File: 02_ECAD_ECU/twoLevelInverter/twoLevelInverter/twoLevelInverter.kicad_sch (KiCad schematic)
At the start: 14 parts, among them J1 FX10A-80S_8-SV_71_, J2 43045-0812, J3 Screw_Terminal_01x04, J4 Screw_Terminal_01x04, J5 Screw_Terminal_01x02, J6 Screw_Terminal_01x02, J7 Screw_Terminal_01x02

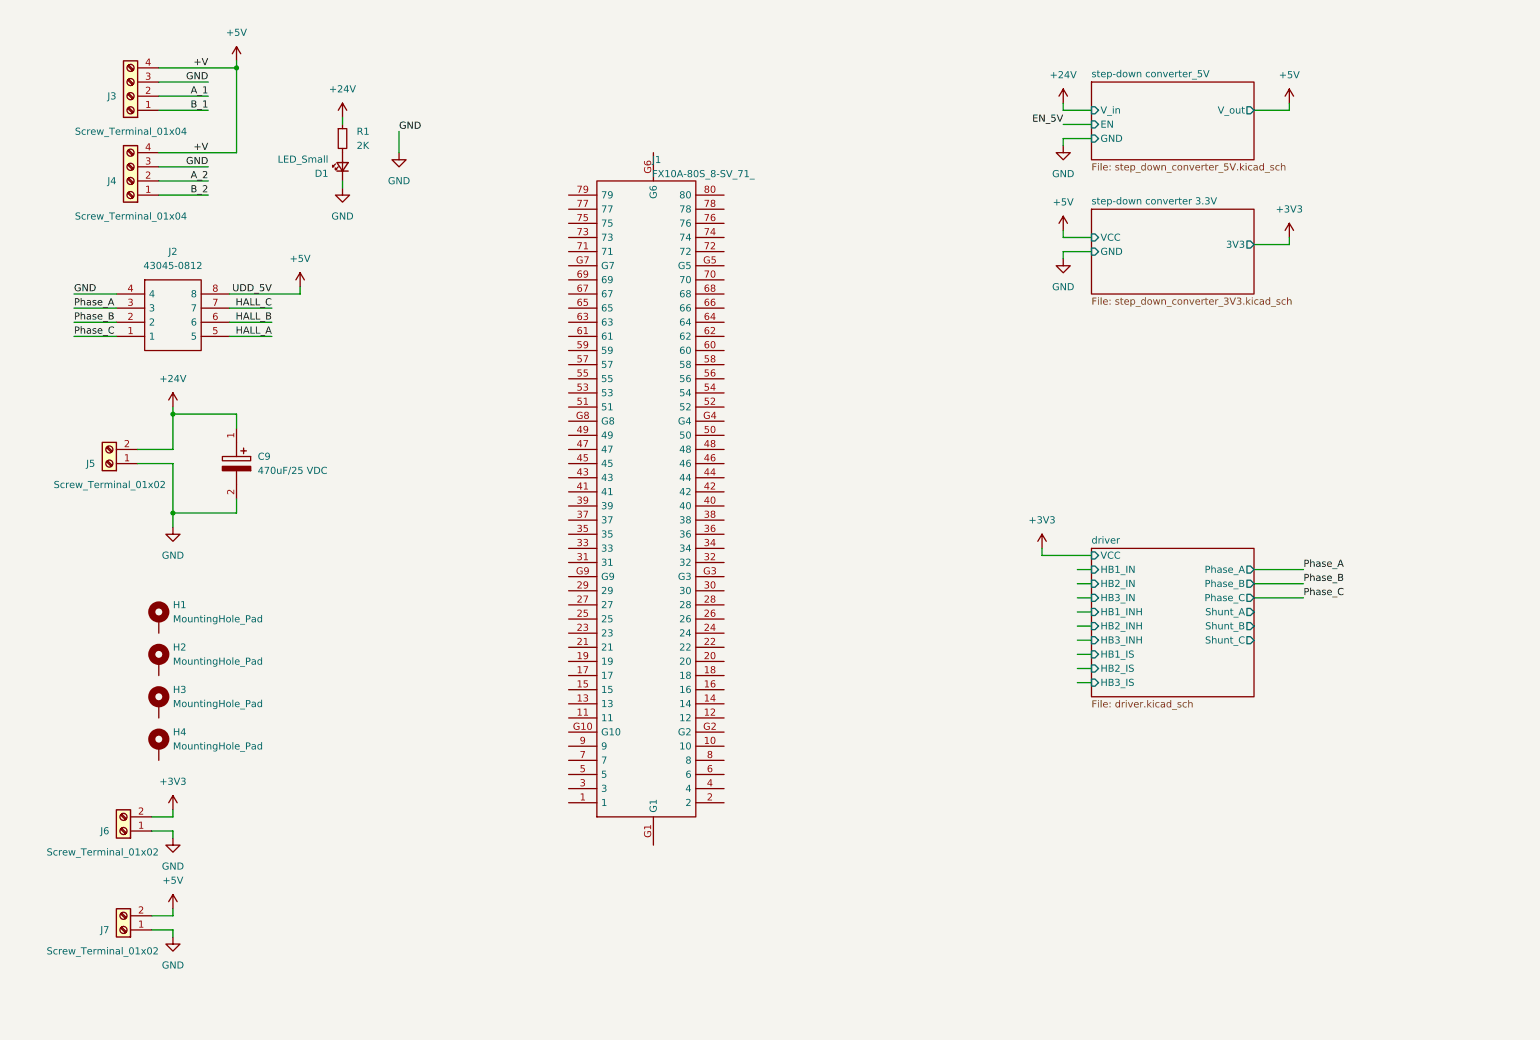
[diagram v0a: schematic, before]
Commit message: encoder, pwm, hall signals mapped
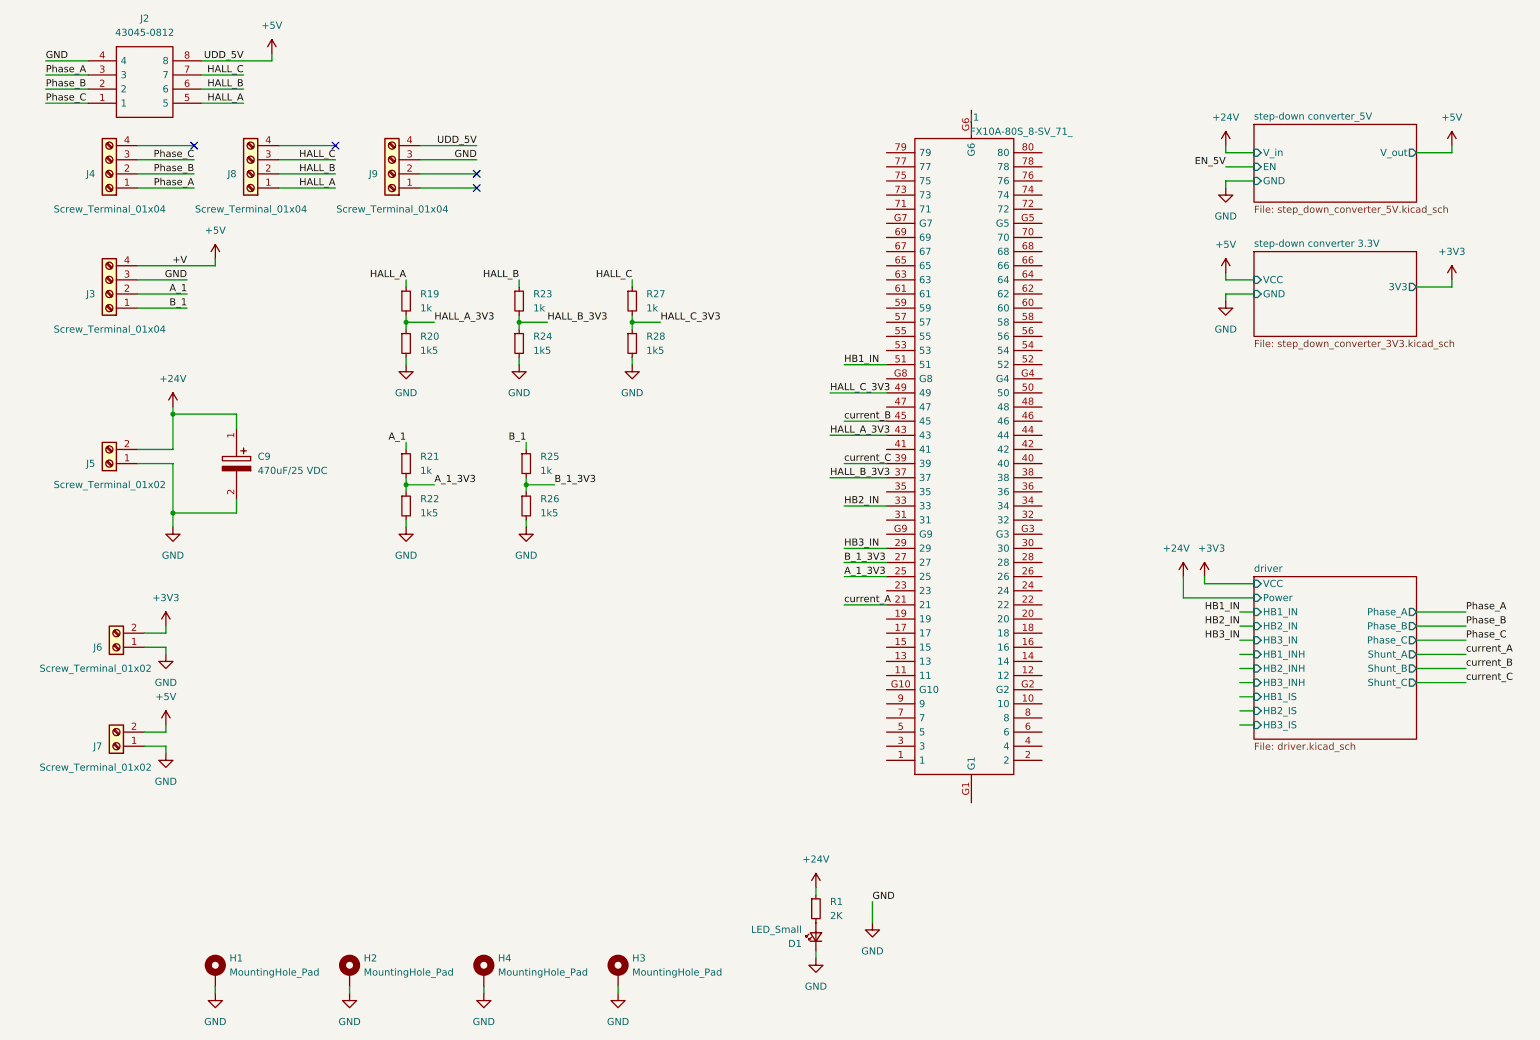
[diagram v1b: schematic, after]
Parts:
- added J8, J9: Screw_Terminal_01x04, TerminalBlock_Phoenix:TerminalBlock_Phoenix_PT-1,5-4-3.5-H_1x04_P3.50mm_Horizontal, symbol Connector:Screw_Terminal_01x04
- added R19, R21, R23, R25, R27: 1k, Resistor_SMD:R_1206_3216Metric, symbol Device:R_Small
- added R20, R22, R24, R26, R28: 1k5, Resistor_SMD:R_1206_3216Metric, symbol Device:R_Small
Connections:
- net A_2 is gone; now on net Phase_B: J4.2 (Pin_2)
- net B_2 is gone; now on net Phase_A: J4.1 (Pin_1)
- net +5V: now also J9.4 (Pin_4); no longer J4.4 (Pin_4)
- net A_1: now also R21.1
- net B_1: now also R25.1
- net GND: now also H1.1, H2.1, H3.1, H4.1, J9.3 (Pin_3), R20.2, R22.2, R24.2, R26.2, R28.2; no longer J4.3 (Pin_3)
- net HALL_A: now also J8.1 (Pin_1), R19.1
- net HALL_B: now also J8.2 (Pin_2), R23.1
- net HALL_C: now also J8.3 (Pin_3), R27.1
- net Phase_C: now also J4.3 (Pin_3)
- net current_A: now reaches J1.21
- net A_1_3V3: now reaches J1.25
- net A_1_3V3: now also R21.2, R22.1
- net B_1_3V3: now reaches J1.27
- net B_1_3V3: now also R25.2, R26.1
- net HB3_IN: now reaches J1.29
- net HB2_IN: now reaches J1.33
- net HALL_B_3V3: now reaches J1.37
- net HALL_B_3V3: now also R23.2, R24.1
- net current_C: now reaches J1.39
- net HALL_A_3V3: now reaches J1.43
- net HALL_A_3V3: now also R19.2, R20.1
- net current_B: now reaches J1.45
- net HALL_C_3V3: now reaches J1.49
- net HALL_C_3V3: now also R27.2, R28.1
- net HB1_IN: now reaches J1.51
- no-connect marks 0 -> 4
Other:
- sheet driver ports: added Power; removed none
- moved on the sheet: D1, H1, H2, H3, H4, J1, J2, J3, J6, J7, R1

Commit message: V1.0  not reviewed
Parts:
- removed J5, J6, J7: Screw_Terminal_01x02, TerminalBlock_Phoenix:TerminalBlock_Phoenix_PT-1,5-2-5.0-H_1x02_P5.00mm_Horizontal, symbol Connector:Screw_Terminal_01x02
- removed J9: Screw_Terminal_01x04, TerminalBlock_Phoenix:TerminalBlock_Phoenix_PT-1,5-4-3.5-H_1x04_P3.50mm_Horizontal, symbol Connector:Screw_Terminal_01x04
- added J5: Screw_Terminal_01x04, max_KiCAD_lib:screwconnector_4_wuerth, symbol Connector:Screw_Terminal_01x04
- D1: value LED_Small -> 24V
- J3, J4, J8: footprint TerminalBlock_Phoenix:TerminalBlock_Phoenix_PT-1,5-4-3.5-H_1x04_P3.50mm_Horizontal -> max_KiCAD_lib:screwconnector_4_wuerth
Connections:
- net +24V: now also J5.4 (Pin_4)
- net +3V3: now also J5.2 (Pin_2)
- net +5V: now also J8.4 (Pin_4), J5.1 (Pin_1)
- net EN_5V: now also J1.73
- net GND: now also J4.4 (Pin_4), J5.3 (Pin_3)
- net HALL_A_3V3: now also J1.49; no longer J1.43
- net HALL_B_3V3: now also J1.43; no longer J1.37
- net HALL_C_3V3: now also J1.37; no longer J1.49
- net current_A: now also J1.45; no longer J1.21
- net current_B: now also J1.39; no longer J1.45
- net current_C: now also J1.21; no longer J1.39
- net HB2_IS: now reaches J1.15
- net HB3_IS: now reaches J1.17
- net HB1_IS: now reaches J1.7
- net HB3_INH: now reaches J1.75
- net HB2_INH: now reaches J1.77
- net HB1_INH: now reaches J1.79
- no-connect marks 4 -> 0
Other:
- moved on the sheet: C9

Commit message: orderd, added gerber files
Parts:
- D1: footprint LED_SMD:LED_1206_3216Metric -> LED_SMD:LED_0805_2012Metric
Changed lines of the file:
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@@
       (effects (font (size 1.27 1.27)) (justify left))
     )
-    (property "Footprint" "LED_SMD:LED_1206_3216Metric" (id 2) (at 153.67 180.34 90)
+    (property "Footprint" "LED_SMD:LED_0805_2012Metric" (id 2) (at 153.67 180.34 90)
       (effects (font (size 1.27 1.27)) hide)
     )
@@
     )
     (path "/ad3114b9-2c32-4326-8bbc-e373921bee11"
-      (reference "D1") (unit 1) (value "24V") (footprint "LED_SMD:LED_1206_3216Metric")
+      (reference "D1") (unit 1) (value "24V") (footprint "LED_SMD:LED_0805_2012Metric")
     )
     (path "/e553575e-0067-4ab5-b453-29a30e175400/db62a153-afe2-405a-b63d-42a0ac7372e4"
@@
     )
     (path "/e553575e-0067-4ab5-b453-29a30e175400/91d46892-a81d-4160-bad4-2aec99acb506"
-      (reference "U1") (unit 1) (value "5V") (footprint "LED_SMD:LED_1206_3216Metric")
+      (reference "U1") (unit 1) (value "5V") (footprint "LED_SMD:LED_0805_2012Metric")
     )
     (path "/e553575e-0067-4ab5-b453-29a30e175400/53da76c1-3035-40bc-8b60-6180b9962a37"
@@
     )
     (path "/e5267c2d-04cf-4f91-8cc8-fffe6b501613/1aa11fbd-fd99-4d92-b287-9585558e457c"
-      (reference "U14") (unit 1) (value "3V3") (footprint "LED_SMD:LED_1206_3216Metric")
+      (reference "U14") (unit 1) (value "3V3") (footprint "LED_SMD:LED_0805_2012Metric")
     )
     (path "/e5267c2d-04cf-4f91-8cc8-fffe6b501613/47c83a27-48b8-49c8-88e0-89bbac668535"
